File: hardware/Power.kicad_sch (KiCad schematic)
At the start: 35 parts, among them IC1 3.3V/0.6A, IC2 TPS54202HDDCR, U12 LMR33640DDDA

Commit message: new beginings tbc
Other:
- note removed: "USB 5V"
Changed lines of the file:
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@@
-		)
-	)
-	(text "USB 5V"
-		(exclude_from_sim no)
-		(at 66.04 87.63 0)
-		(effects
-			(font
-				(size 5 5)
-				(thickness 1)
-				(bold yes)
-			)
-			(justify left bottom)
 		)
 	)

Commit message: sync
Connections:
- net SW_5V: no longer C10.2, L2.1, U12.8 (SW)
- new net SW_12V: C10.2, L2.1, U12.8 (SW)
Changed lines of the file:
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@@
 		)
 	)
-	(label "SW_5V"
+	(label "SW_12V"
 		(at 102.87 158.75 0)
 		(fields_autoplaced yes)
@@
 	)
 	(symbol
+		(lib_name "GND_4")
 		(lib_id "power:GND")
 		(at 58.42 114.3 0)
@@
 	)
 	(symbol
+		(lib_name "+5V_2")
 		(lib_id "power:+5V")
 		(at 62.23 31.75 0)
@@
 	)
 	(symbol
+		(lib_name "Fuse_Small_1")
 		(lib_id "Device:Fuse_Small")
 		(at 115.57 101.6 180)
@@
 	)
 	(symbol
+		(lib_name "GND_3")
 		(lib_id "power:GND")
 		(at 105.41 54.61 0)
@@
 	)
 	(symbol
+		(lib_name "GND_2")
 		(lib_id "power:GND")
 		(at 144.78 179.07 0)
@@
 	)
 	(symbol
+		(lib_name "GND_1")
 		(lib_id "power:GND")
 		(at 110.49 114.3 0)
@@
 	)
 	(symbol
+		(lib_name "VDD_1")
 		(lib_id "power:VDD")
 		(at 44.45 146.05 0)
@@
 	)
 	(symbol
+		(lib_name "VDD_2")
 		(lib_id "power:VDD")
 		(at 171.45 60.96 0)
@@
 	)
 	(symbol
+		(lib_name "+5V_1")
 		(lib_id "power:+5V")
 		(at 124.46 99.06 0)
@@
 	)
 	(symbol
+		(lib_name "Fuse_Small_2")
 		(lib_id "Device:Fuse_Small")
 		(at 62.23 36.83 270)

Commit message: schematic done
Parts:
- removed C15: 100nF, Capacitor_SMD:C_0603_1608Metric, symbol Device:C_Small
- removed D14: RB068LAM-30TFTR, Diode_SMD:D_SOD-123, symbol Device:D_Schottky_Small
- removed F3: 16V/0.5A, Fuse:Fuse_1210_3225Metric, symbol Device:Fuse_Small
- removed L1: 4.7uH, Inductor_SMD:L_1206_3216Metric, symbol Device:L_Small
- added D14: D_TVS_Small, Diode_SMD:D_SOD-123, symbol Device:D_TVS_Small
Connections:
- net GND: now also D14.1 (A1)
- net at C12.2, C17.2, C21.2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: now also D14.2 (A2)
- net +3V3 renamed +3.3V
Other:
- note added: "12V"
- note added: "3.3V"
- note added: "5V"
- moved on the sheet: C10, C11, C12, C13, C14, C16, C17, C19, C20, C21, C22, C26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

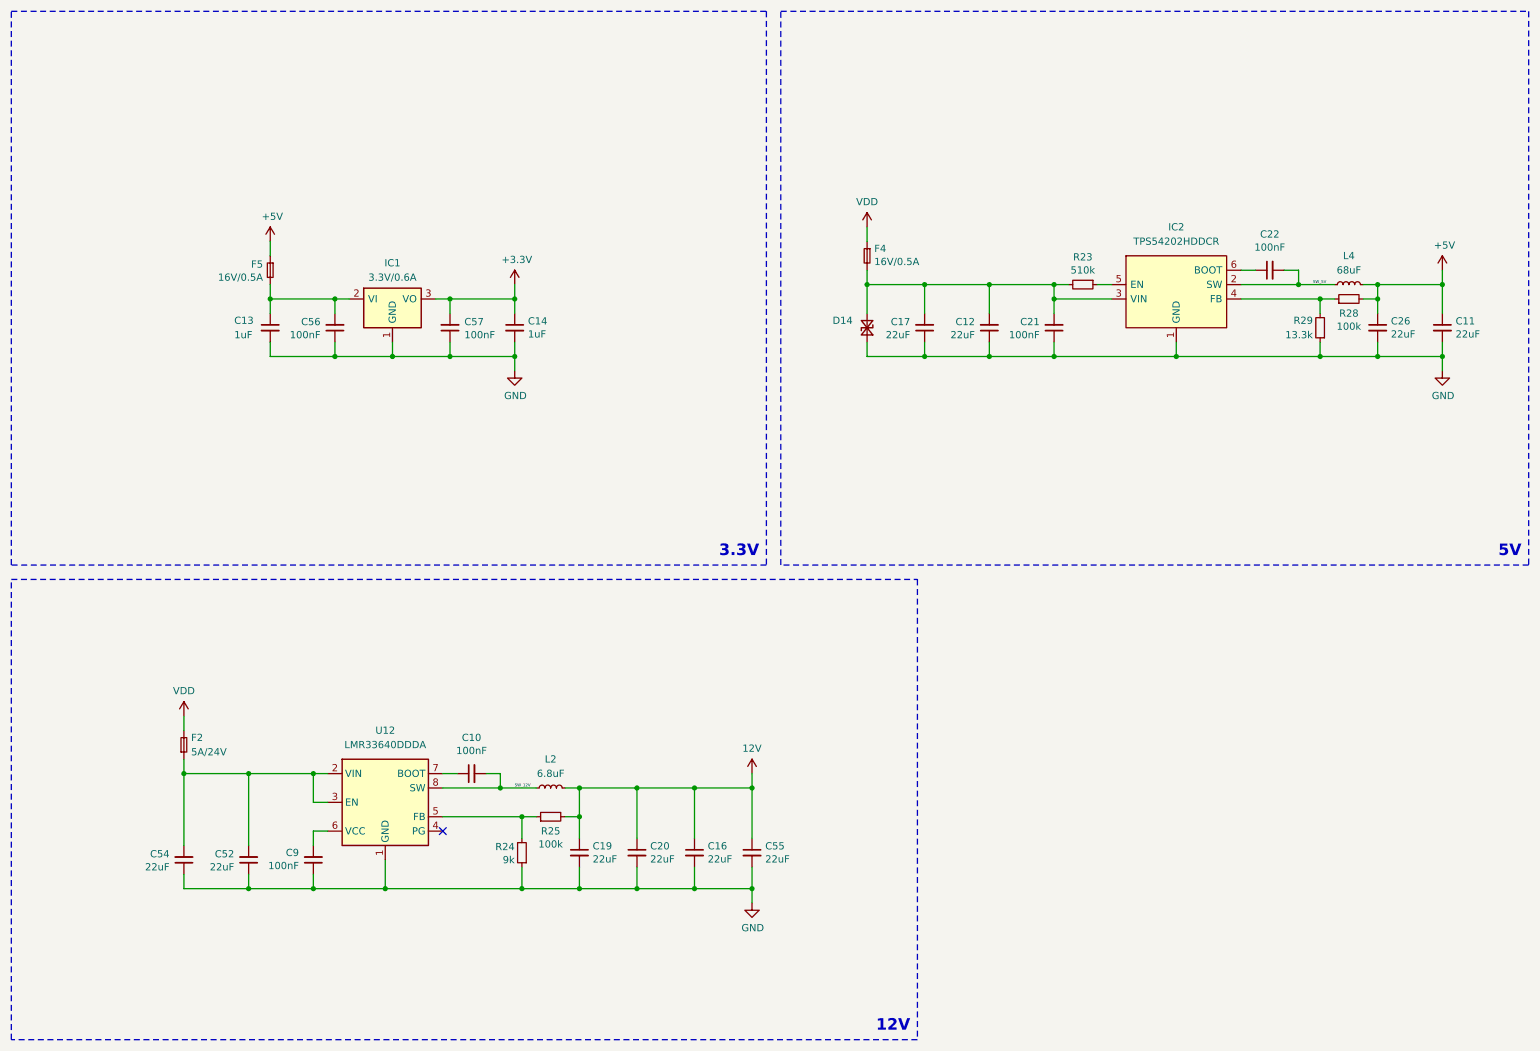
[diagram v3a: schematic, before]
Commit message: new firmware for bga version of stm, change stm from smt to bga, smaller HV dividers, added 3rd can transciver, and other
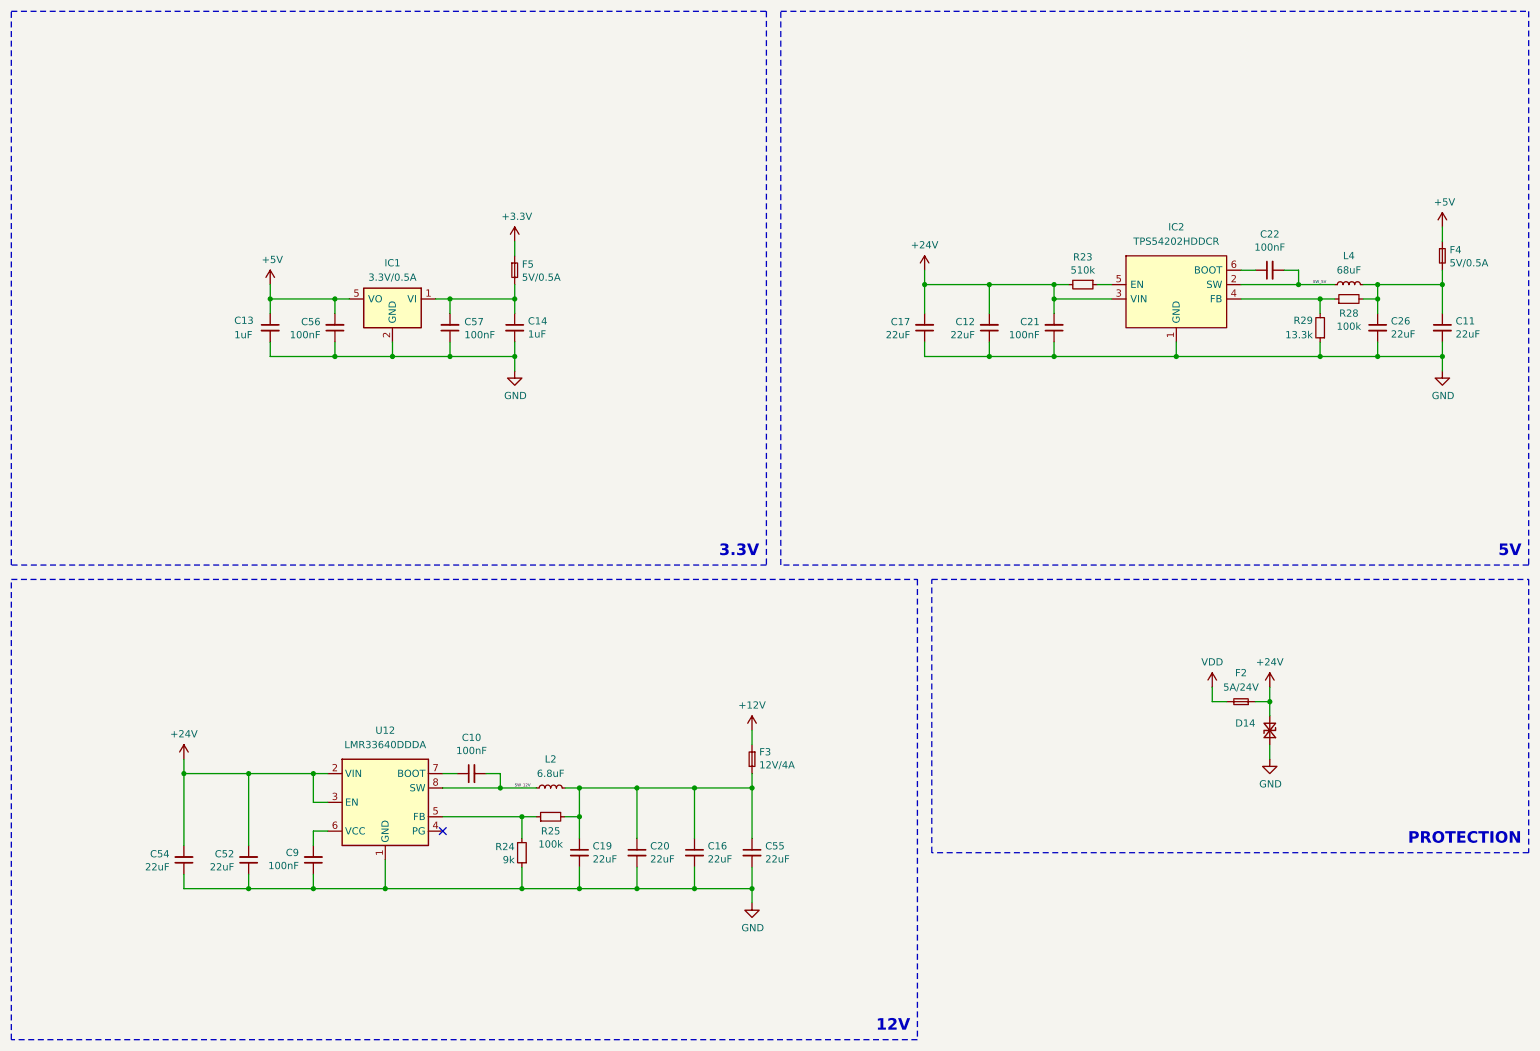
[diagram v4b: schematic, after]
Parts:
- added F3: 12V/4A, Fuse:Fuse_1206_3216Metric, symbol Device:Fuse_Small
- F4, F5: value 16V/0.5A -> 5V/0.5A; footprint Fuse:Fuse_1210_3225Metric -> Fuse:Fuse_0805_2012Metric
- IC1: value 3.3V/0.6A -> 3.3V/0.5A; footprint Package_TO_SOT_SMD:SOT-89-3 -> Package_TO_SOT_SMD:SOT-23-5; Manufacturer_Name Diodes Inc. -> Texas Instruments; Manufacturer_Part_Number AP7365-33YRG-13 -> TPS7B92033DBVR; Mouser Part Number 621-AP7365-33YRG-13 -> 595-TPS7B92033DBVR; Mouser Price/Stock https://www.mouser.co.uk/ProductDetail/Diodes-Incorporated/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 -> https://www.mouser.pl/ProductDetail/Texas-Instruments/TPS7B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
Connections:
- net +3.3V: now also F5.1; no longer C14.1, C57.2, IC1.3 (VO)
- net +5V: now also C13.1, C56.2, F4.1, IC1.5 (VO); no longer C11.1, C26.1, F5.1, L4.2, R28.2
- net GND: now also IC1.2 (GND); no longer IC1.1 (GND)
- net VDD: no longer F4.1
- net +24V: now reaches C12.2, C17.2, C21.2, D14.2 (A2), IC2.3 (VIN), R23.2
- net +24V: now also C52.2, C54.2, F2.1, U12.2 (VIN), U12.3 (EN); no longer F4.2
- net 12V: no longer names the net of C16.1, C19.1, C20.1, C55.1, L2.2, R25.2
- net 12V: now also F3.2
- new net: C14.1, C57.2, F5.2, IC1.1 (VI)
- new net: C11.1, C26.1, F4.2, L4.2, R28.2
- new net: IC1.3 (NC), IC1.4 (NC)
- new net +12V: F3.1
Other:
- note added: "PROTECTION"
- moved on the sheet: D14, F2, F5

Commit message: mcu pinout done
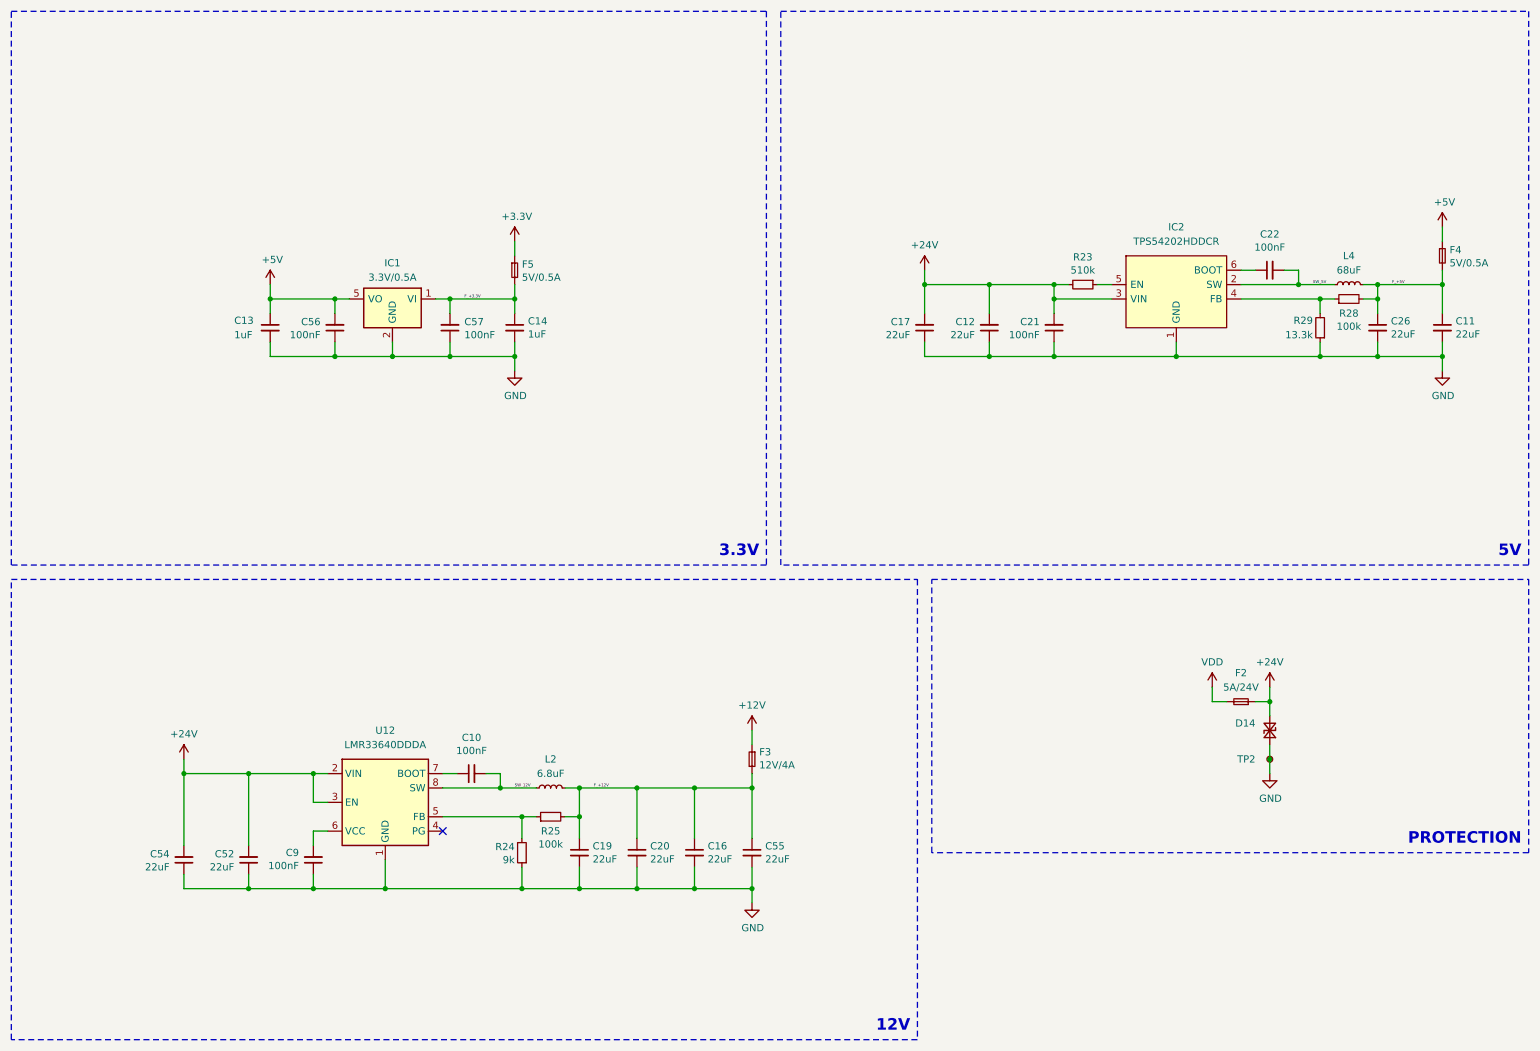
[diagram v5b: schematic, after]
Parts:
- added TP2: TestPoint_Small, Connector_Pin:Pin_D0.7mm_L6.5mm_W1.8mm_FlatFork, symbol Connector:TestPoint_Small
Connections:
- net GND: now also TP2.1
- net F_+12V: now reaches C16.1, C19.1, C20.1, C55.1, F3.2, L2.2, R25.2
- net F_+3.3V: now reaches C14.1, C57.2, F5.2, IC1.1 (VI)
- net F_+5V: now reaches C11.1, C26.1, F4.2, L4.2, R28.2
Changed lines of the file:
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@@
 	)
 	(junction
-		(at 266.7 62.23)
-		(diameter 0)
-		(color 0 0 0 0)
-	)
-	(junction
 		(at 81.28 74.93)
 		(diameter 0)
@@
 	)
 	(junction
+		(at 266.7 62.23)
+		(diameter 0)
+		(color 0 0 0 0)
+	)
+	(junction
 		(at 114.3 168.91)
 		(diameter 0)
@@
 		(color 0 0 0 0)
 	)
+	(junction
+		(at 236.22 146.05)
+		(diameter 0)
+		(color 0 0 0 0)
+	)
 	(no_connect
 		(at 90.17 158.75)
@@
 	(wire
 		(pts
+			(xy 236.22 146.05) (xy 236.22 148.59)
+		)
+		(stroke
+			(width 0)
+			(type default)
+		)
+	)
+	(wire
+		(pts
 			(xy 231.14 64.77) (xy 245.11 64.77)
 		)
@@
 	(wire
 		(pts
-			(xy 266.7 62.23) (xy 266.7 67.31)
+			(xy 266.7 59.69) (xy 266.7 62.23)
 		)
 		(stroke
@@
 	(wire
 		(pts
-			(xy 266.7 59.69) (xy 266.7 62.23)
+			(xy 111.76 151.13) (xy 114.3 151.13)
 		)
 		(stroke
@@
 	(wire
 		(pts
-			(xy 111.76 151.13) (xy 114.3 151.13)
+			(xy 198.12 74.93) (xy 198.12 72.39)
 		)
 		(stroke
@@
 	(wire
 		(pts
-			(xy 198.12 74.93) (xy 198.12 72.39)
+			(xy 266.7 62.23) (xy 266.7 67.31)
 		)
 		(stroke
@@
 		)
 	)
+	(label "F_+5V"
+		(at 257.81 62.23 0)
+		(fields_autoplaced yes)
+		(effects
+			(font
+				(size 0.5 0.5)
+			)
+			(justify left bottom)
+		)
+	)
 	(label "SW_5V"
 		(at 243.84 62.23 0)
@@
 		)
 	)
+	(label "F_+3.3V"
+		(at 93.98 64.77 0)
+		(fields_autoplaced yes)
+		(effects
+			(font
+				(size 0.5 0.5)
+			)
+			(justify left bottom)
+		)
+	)
+	(label "F_+12V"
+		(at 116.84 151.13 0)
+		(fields_autoplaced yes)
+		(effects
+			(font
+				(size 0.5 0.5)
+			)
+			(justify left bottom)
+		)
+	)
 	(symbol
 		(lib_id "Device:C_Small")
@@
 	)
 	(symbol
+		(lib_id "Connector:TestPoint_Small")
+		(at 236.22 146.05 0)
+		(unit 1)
+		(exclude_from_sim no)
+		(in_bom yes)
+		(on_board yes)
+		(dnp no)
+		(property "Reference" "TP2"
+			(at 233.68 146.05 0)
+			(effects
+				(font
+					(size 1.27 1.27)
+				)
+				(justify right)
+			)
+		)
+		(property "Value" "TestPoint_Small"
+			(at 237.49 147.3199 0)
+			(effects
+				(font
+					(size 1.27 1.27)
+				)
+				(justify left)
+				(hide yes)
+			)
+		)
+		(property "Footprint" "Connector_Pin:Pin_D0.7mm_L6.5mm_W1.8mm_FlatFork"
+			(at 241.3 146.05 0)
+			(effects
+				(font
+					(size 1.27 1.27)
+				)
+				(hide yes)
+			)
+		)
+		(property "Datasheet" "~"
+			(at 241.3 146.05 0)
+			(effects
+				(font
+					(size 1.27 1.27)
+				)
+				(hide yes)
+			)
+		)
+		(property "Description" "test point"
+			(at 236.22 146.05 0)
+			(effects
+				(font
+					(size 1.27 1.27)
+				)
+				(hide yes)
+			)
+		)
+		(pin "1"
+		)
+		(instances
+			(project "PUTM_EV_BMS_HV_MASTER_2023"
+				(path "/b456cffc-d9d7-4c91-91f2-36ec9a65dd1b/66c3869d-de11-4d8d-b4de-9d98c32ec205"
+					(reference "TP2")
+					(unit 1)
+				)
+			)
+		)
+	)
+	(symbol
 		(lib_name "GND_3")
 		(lib_id "power:GND")
@@
 	(symbol
 		(lib_id "power:GND")
-		(at 236.22 146.05 0)
+		(at 236.22 148.59 0)
 		(unit 1)
 		(exclude_from_sim no)
@@
 		(dnp no)
 		(property "Reference" "#PWR091"
-			(at 236.22 152.4 0)
+			(at 236.22 154.94 0)
 			(effects
 				(font
@@
 		)
 		(property "Value" "GND"
-			(at 236.347 150.4442 0)
+			(at 236.347 152.9842 0)
 			(effects
 				(font
@@
 		)
 		(property "Footprint" ""
-			(at 236.22 146.05 0)
+			(at 236.22 148.59 0)
 			(effects
 				(font
@@
 		)
 		(property "Datasheet" ""
-			(at 236.22 146.05 0)
+			(at 236.22 148.59 0)
 			(effects
 				(font
@@
 		)
 		(property "Description" ""
-			(at 236.22 146.05 0)
+			(at 236.22 148.59 0)
 			(effects
 				(font

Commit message: mama comit
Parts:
- removed D14: D_TVS_Small, Diode_SMD:D_SOD-123, symbol Device:D_TVS_Small
- added C3, C4, C5, C6: 22uF, Capacitor_SMD:C_0805_2012Metric, symbol Device:C_Small
- added D14: 6V, symbol Device:D_Zener_Small
- added D16: 30V, symbol Device:D_Zener_Small
- added D8: 0.5/1A, symbol Device:D_Small
- added F8: 5V/0.5A, Fuse:Fuse_0805_2012Metric, symbol Device:Fuse_Small
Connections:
- net +24V: now also D16.1 (K)
- net +5V: now also F8.1
- net GND: now also C3.1, C4.1, C5.1, C6.1, D14.2 (A), D16.2 (A)
- new net: C4.2, C5.2, D8.1 (K), F8.2
- new net VBUS+: C3.2, C6.2, D14.1 (K), D8.2 (A)
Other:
- note added: "USB +5V"
- moved on the sheet: C13, C14, C56, C57, F5, IC1
